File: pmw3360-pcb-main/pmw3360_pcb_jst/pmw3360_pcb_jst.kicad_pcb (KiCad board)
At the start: 2 copper layers, 27 x 28 mm, 20 parts, among them J1 Conn_01x08, U1 PMW3360DM-T2QU, U2 TLV74318PDBVR

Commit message: gerbers for production
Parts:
- C4: value 4.7uF -> 1uF
- moved C5 0.82 mm to (191.6, 140.9)
- moved R4 0.82 mm to (191.6, 139.1)
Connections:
- H1 pad 1: GND -> unconnected-(H1-Pad1)
- H2 pad 1: GND -> unconnected-(H2-Pad1)
- H3 pad 1: GND -> unconnected-(H3-Pad1)
- H4 pad 1: GND -> unconnected-(H4-Pad1)
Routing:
- net GND: track 12.7 -> 13.7 mm, vias 9 -> 24
- net Net-(U2-NC): track 8.11 -> 8.75 mm
- net V_{IN}: track 49.5 -> 50.1 mm

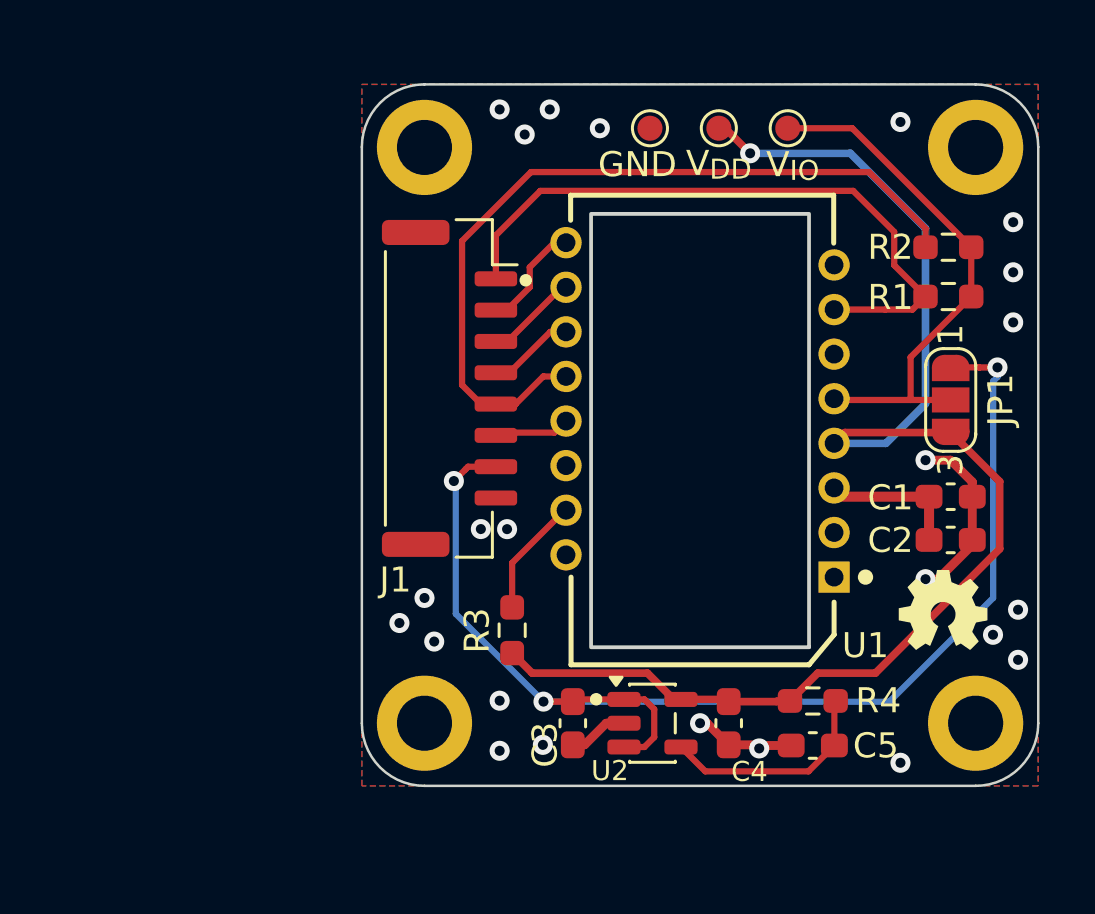
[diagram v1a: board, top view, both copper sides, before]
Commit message: mouse sensor bots libraries
- footprints not done yet. shematics yes.
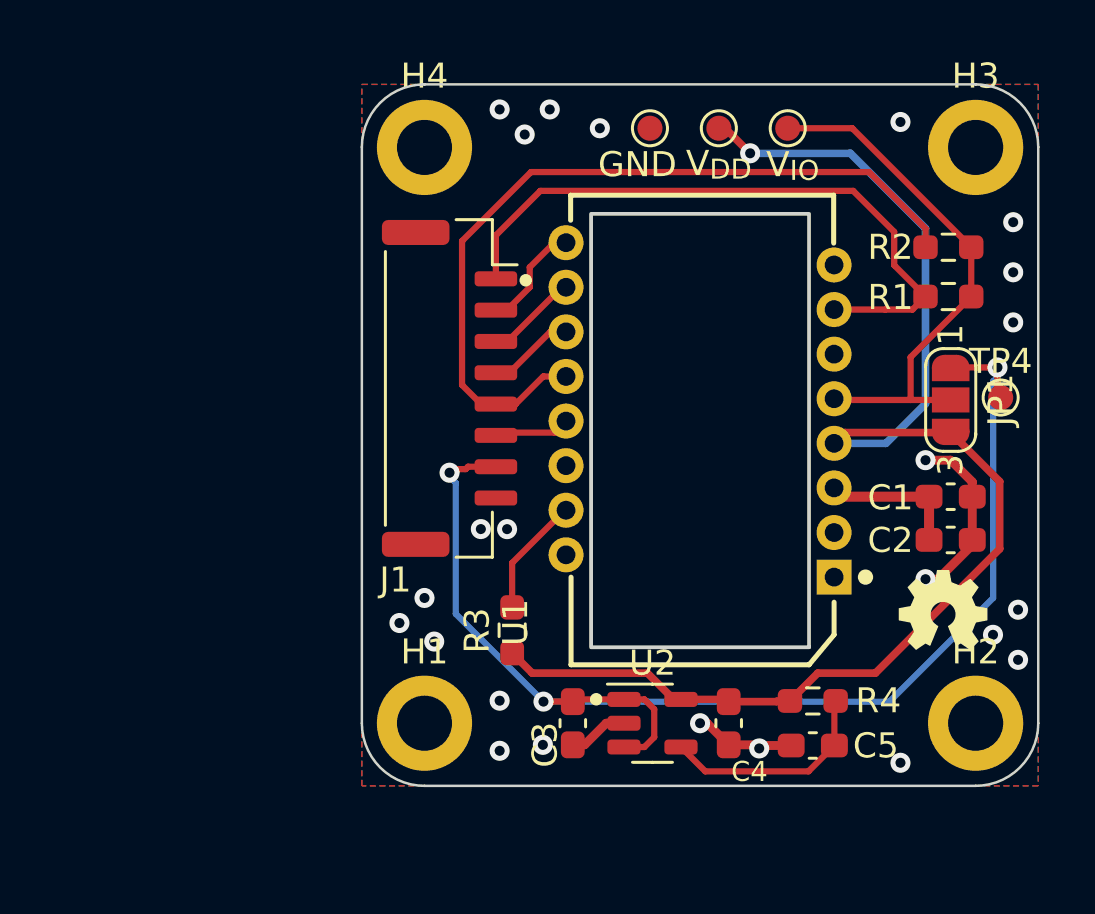
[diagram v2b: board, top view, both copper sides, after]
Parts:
- added TP4: 1.0mm, TestPoint:TestPoint_Pad_D1.0mm, F.Cu at (199.1, 127.0)
- C1: value 4.7uF/10V -> 4.7uF_HS
- C2: value 100nF -> 0.1uF_HS
- C3, C4: value 1uF -> 1uF_HS
- C5: value 22nF -> 22nF_HS
- H1, H2, H3, H4: value MountingHole_Pad -> M2; footprint MountingHole:MountingHole_2.2mm_M2_ISO14580_Pad -> bots:MountingHole_2.2mm_M2_ISO14580_Pad
- J1: value Conn_01x08 -> JST_SM08B-GHS-TB
- R1, R2: value 10k -> 10k_HS
- R3: value 39R -> R
- R4: value 28k -> 10k_HS
- TP1: value V_{IO} -> 1.0mm
- TP2: value V_{DD} -> 1.0mm
- TP3: value GND -> 1.0mm
- U1: value PMW3360DM-T2QU -> IC_PMW3360DM-T2QU; footprint PMW3360_PCB:PMW3360DM-T2QU 16Pin -> bots:IC_PMW3360DM-T2QU 16Pin
- U2: value TLV74318PDBVR -> LDO_TLV74318PDBVR; footprint Package_TO_SOT_SMD:SOT-23-5 -> bots:SOT-23-5
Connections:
- net V_{IN} renamed +5V
- J1 pad MP: (no net) -> unconnected-(J1-PadMP)_1
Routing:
- net +5V: track 50.1 -> 51.8 mm

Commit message: 3dmodels + footprints
- one resistor unvalued + no footprint
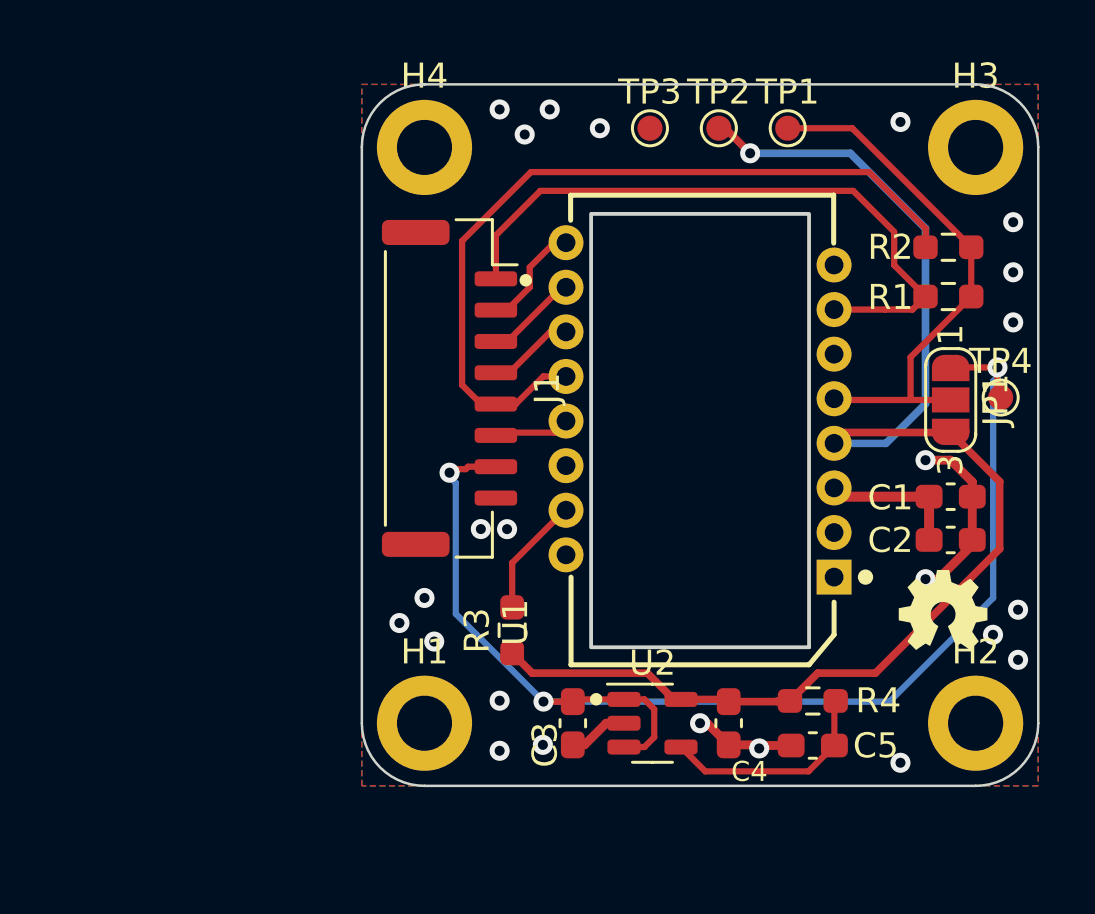
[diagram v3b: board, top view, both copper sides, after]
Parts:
- J1: footprint Connector_JST:JST_GH_SM08B-GHS-TB_1x08-1MP_P1.25mm_Horizontal -> bots:JST_GH_SM08B-GHS-TB_1x08-1MP_P1.25mm_Horizontal
- JP1: footprint Jumper:SolderJumper-3_P1.3mm_Open_RoundedPad1.0x1.5mm_NumberLabels -> bots:SolderJumper-3_P1.3mm_Open_RoundedPad1.0x1.5mm_NumberLabels
- TP1, TP2, TP3, TP4: footprint TestPoint:TestPoint_Pad_D1.0mm -> bots:TestPoint_Pad_D1.0mm

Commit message: libraries and stuff
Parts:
- added G***: LOGO, bots:SILK_BotsLogo_Small, F.Cu at (164.6, 144.0)
- added REF**: SILK_BotsLogo_Small, bots:SILK_BotsLogo_Small, B.Cu at (163.1, 137.0)
- C1, C2, C3, C4, C5: footprint Capacitor_SMD:C_0603_1608Metric_Pad1.08x0.95mm_HandSolder -> bots:C_0603_1608Metric_Pad1.08x0.95mm_HandSolder
- R1, R2, R4: footprint Resistor_SMD:R_0603_1608Metric_Pad0.98x0.95mm_HandSolder -> bots:R_0603_1608Metric_Pad0.98x0.95mm_HandSolder
- R3: value R -> 39R_HS; footprint Resistor_SMD:R_0603_1608Metric_Pad0.98x0.95mm_HandSolder -> bots:R_0603_1608Metric_Pad0.98x0.95mm_HandSolder
- VIN (5V): renamed from TP4
- renumbered TP3 to GND, TP2 to VDD, TP1 to VIO
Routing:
- net VDD: track 53.8 -> 55.0 mm
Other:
- board text added: "The Bots Mouse Sensor PCB PMW3360 PCB Rev J.1 Mod by: Akhil V. and Henry B."
- board text removed: "${TITLE} Rev ${REVISION}"

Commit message: mouse_sensorV1 prod done
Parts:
- removed the G*** at (164.6, 144.0)
- removed the REF** at (163.1, 137.0)
- added G***: LOGO, bots:SILK_BotsLogo_VerySmall, F.Cu at (196.6, 136.5)
- added REF**: SILK_TheBotsLogo_Small, bots:SILK_TheBotsLogo_Small, B.Cu at (198.3, 129.7)
- J1: footprint bots:JST_GH_SM08B-GHS-TB_1x08-1MP_P1.25mm_Horizontal -> bots:JST_BM08B-GHS-TBT_LF__SN__N_
- moved J1 1.85 mm to (179.0, 126.7)
- moved VIN (5V) 0.37 mm to (199.5, 126.8)
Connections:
- J1 pad MP: unconnected-(J1-PadMP)_1 -> (no net)

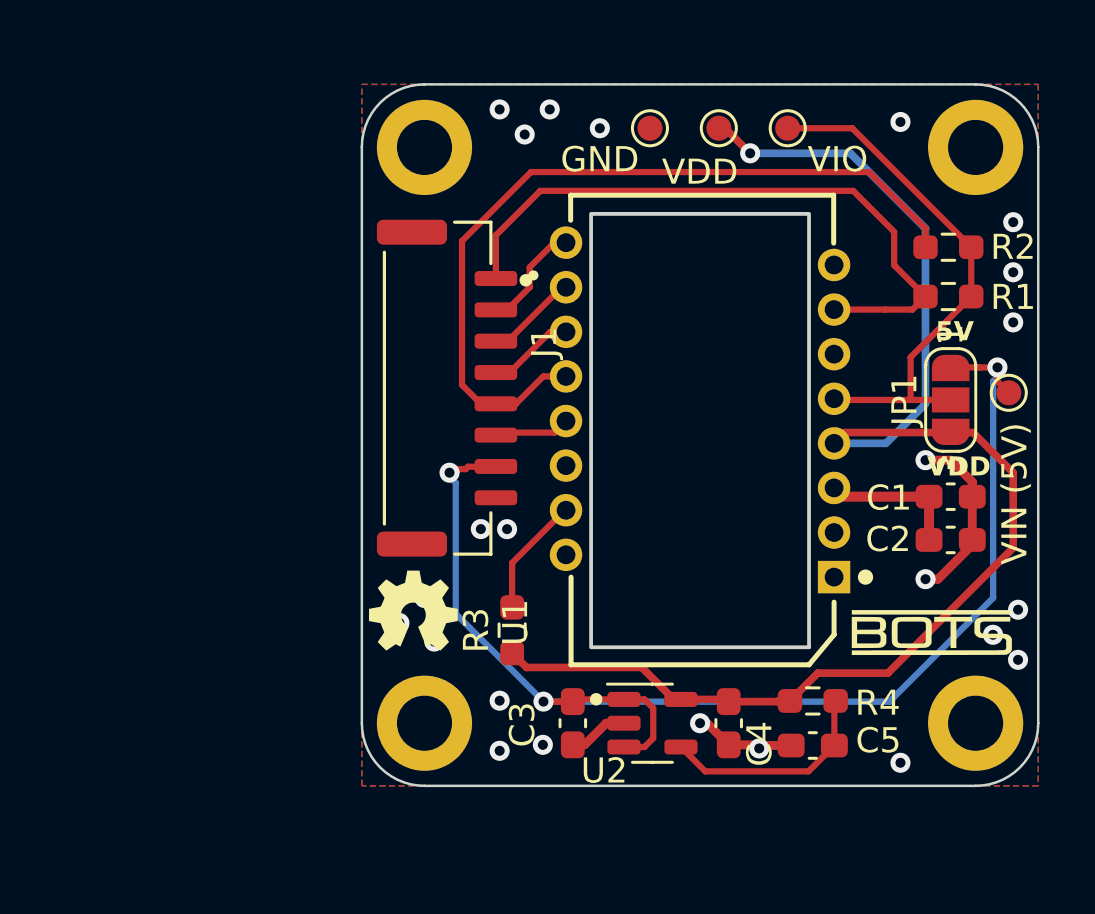
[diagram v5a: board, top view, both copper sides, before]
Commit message: production files - working
- modified board slightly, added 3d models, added part numbers for JLC
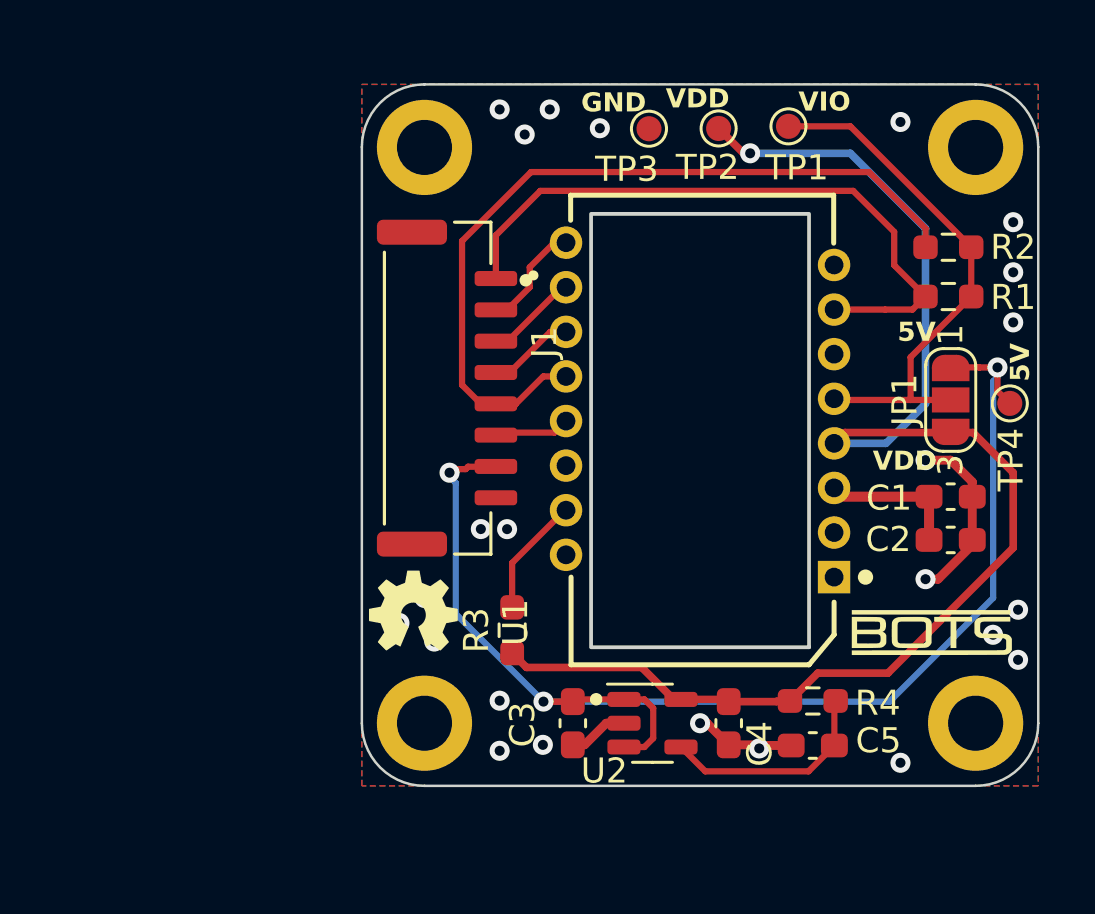
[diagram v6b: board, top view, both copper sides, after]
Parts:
- removed GND, VDD, VIO: 1.0mm, bots:TestPoint_Pad_D1.0mm
- removed VIN (5V): 1.0mm, bots:TestPoint_Pad_D1.0mm
- added TP1: 1.0mm, bots:TestPoint_Pad_D1.0mm, F.Cu at (190.7, 116.2)
- added TP2: 1.0mm, bots:TestPoint_Pad_D1.0mm, F.Cu at (187.9, 116.3)
- added TP3: 1.0mm, bots:TestPoint_Pad_D1.0mm, F.Cu at (185.1, 116.3)
- added TP4: 1.0mm, bots:TestPoint_Pad_D1.0mm, F.Cu at (199.5, 127.3)
- J1: value JST_SM08B-GHS-TB -> JST_BM08B-GHS-TBT
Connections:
- J1 pad MP: (no net) -> unconnected-(J1-PadMP)_1
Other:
- board text added: "5V"
- board text added: "VDD"
- board text added: "VIO"
